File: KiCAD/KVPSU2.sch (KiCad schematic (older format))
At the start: 24 parts

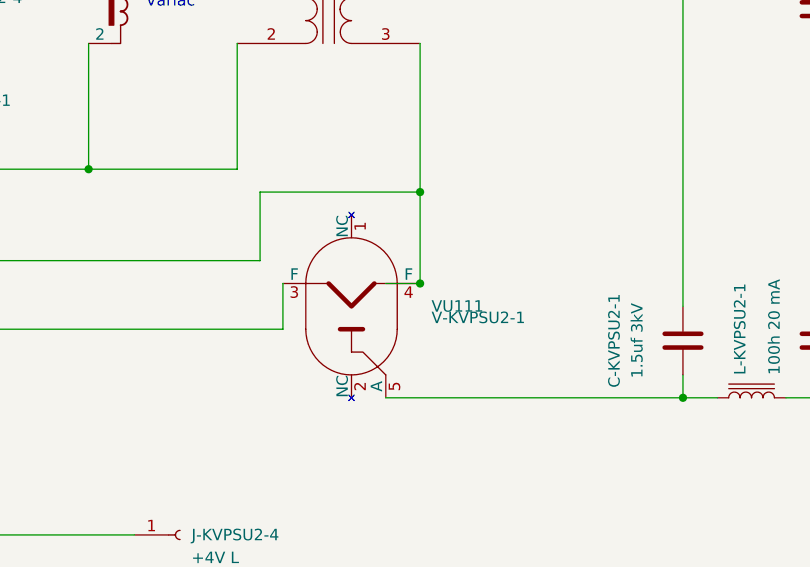
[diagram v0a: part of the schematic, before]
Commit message: Finish powrctl6b
Likely wrong bit of it I didn't understand other bits seem wrong inthe orginal.



Signed-off-by: John Bradley <flypie@rocketmail.com>
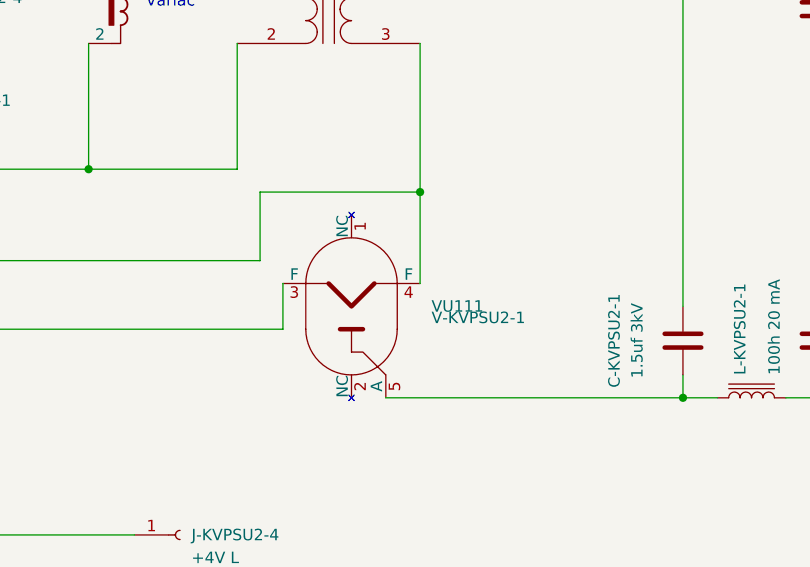
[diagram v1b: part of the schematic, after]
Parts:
- V-KVPSU2-4: footprint Valve:Valve_Octal -> Connector_PinHeader_2.54mm:PinHeader_1x02_P2.54mm_Vertical
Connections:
- wire segments 59 -> 58
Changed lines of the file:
@@
 F 0 "V-KVPSU2-4" H 3350 1250 50  0000 L CNN
 F 1 "CV71" H 3350 1200 50  0000 L CNN
-F 2 "Valve:Valve_Octal" H 3530 1125 50  0001 C CNN
+F 2 "Connector_PinHeader_2.54mm:PinHeader_1x02_P2.54mm_Vertical" H 3530 1125 50  0001 C CNN
 F 3 "http://www.r-type.org/pdfs/cv71.pdf" H 2200 1500 50  0001 C CNN
 	1    3200 1200
@@
 Wire Wire Line
 	3200 950  2900 950
-Wire Wire Line
-	5350 2400 5500 2400
 Wire Wire Line
 	5350 2900 6650 2900
@@
 Text Label 9700 1100 0    50   ~ 0
 GND
-Connection ~ 5500 2400
 Wire Wire Line
 	4900 2400 4900 2600
